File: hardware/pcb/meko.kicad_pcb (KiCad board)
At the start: 2 copper layers, 282 parts, among them IC1 MCP16502AB, IC2 MAYA-W386-00B, IC3 TAC5212, J1 Conn_01x02_Pin, J2 Conn_ARM_JTAG_SWD_10, J3 USB_C_Receptacle_USB2.0_16P, J4 PJ-342, J5 PJ-242, J6 Micro_SD_Card_Det2, J7 Micro_SD_Card_Det1, J8 503480-1000, SW1 SW_Push_Shielded, SW2 SW_Push_Shielded, SW3 SW_Push_Shielded, SW4 SW_Push_Shielded, SW5 SW_Push_Shielded, U1 SAMA7D65-4HB, U2 MT41K256M16TW, U3 TPS7A2033PDBV, U4 BQ25640, U5 MAX17260, U6 ECMF02-2AMX6, U7 DRV2605LDGS, Y1 24MHz, Y2 32kHz768, Y3 32kHz768

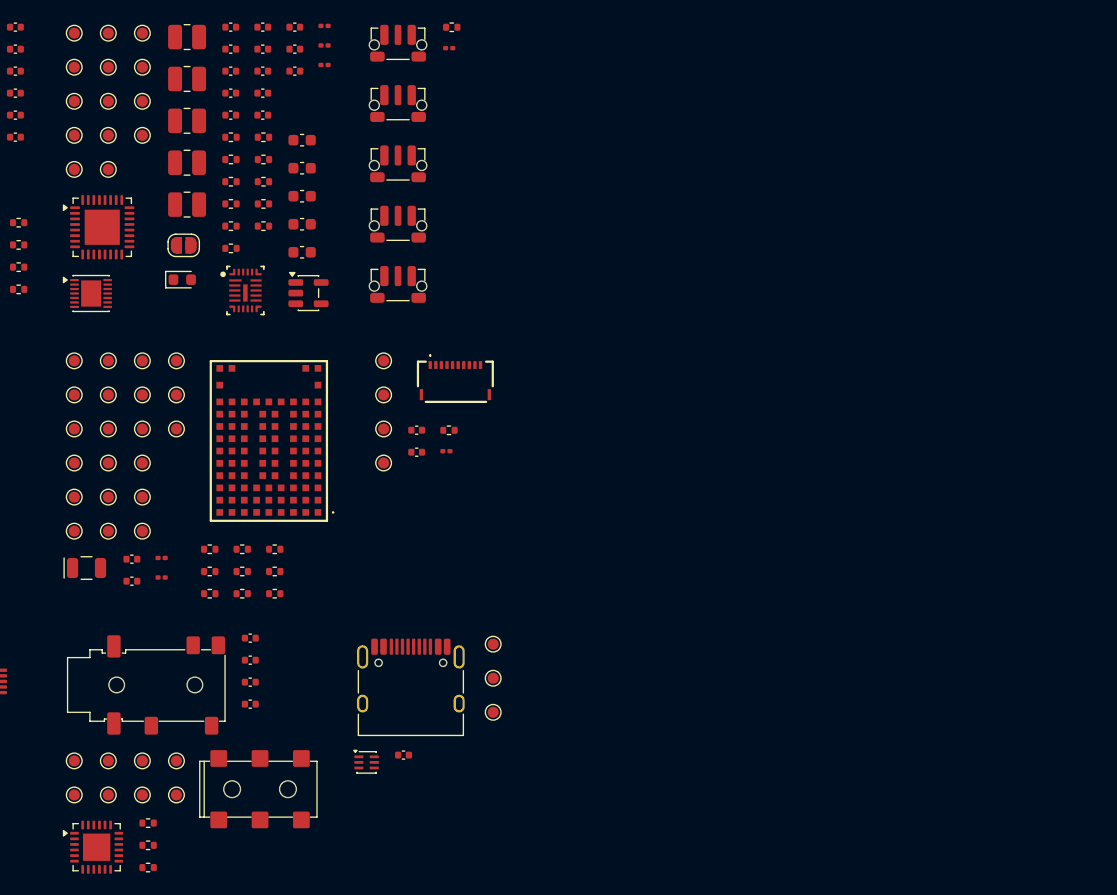
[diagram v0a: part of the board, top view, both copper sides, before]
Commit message: fixed 3.5mm footprint
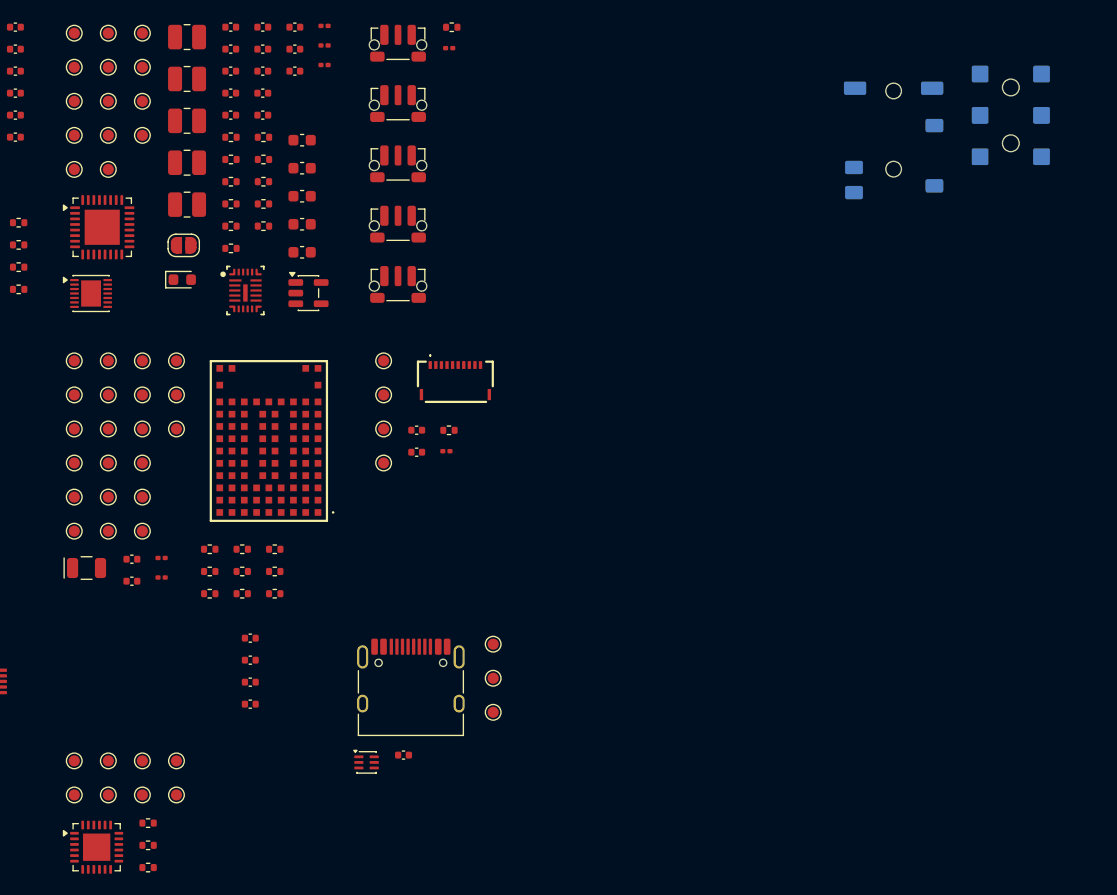
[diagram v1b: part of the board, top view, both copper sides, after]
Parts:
- J4, J5: moved to B.Cu
- moved J5 90.3 mm to (177.3, 61.5), turned to -90 degrees
- moved J4 77.8 mm to (166.8, 66.4), turned to -90 degrees

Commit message: mucking around with layout
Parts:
- IC3, J7: moved to B.Cu
- moved J7 141.6 mm to (205.7, 101.1), turned to -90 degrees
- moved IC2 129.1 mm to (239.4, 78.8)
- moved J6 113.5 mm to (187.8, 60.3), turned to 180 degrees
- moved IC3 96.4 mm to (174.0, 71.1), turned to 180 degrees
- moved U1 88.8 mm to (187.8, 81.5), turned to 0 degrees
- moved R42 88.3 mm to (168.3, 72.8)
- moved R41 88.3 mm to (168.3, 70.9)
- moved J8 79.8 mm to (206.4, 73.2), turned to -90 degrees
- moved U2 69.6 mm to (174.5, 97.9)
- moved J3 63.5 mm to (185.9, 125.7)
- moved J5 0.76 mm to (176.6, 61.5)
- moved J4 0.76 mm to (166.1, 66.3)

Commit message: doing layout
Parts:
- J3, SW2, SW3, SW4, SW5: moved to B.Cu
- moved SW5 138.4 mm to (213.7, 181.0), turned to -90 degrees
- moved SW3 122.6 mm to (213.8, 147.8), turned to -90 degrees
- moved SW4 118.2 mm to (166.8, 181.0), turned to 90 degrees
- moved SW2 118.0 mm to (213.7, 135.6), turned to -90 degrees
- moved J3 72.8 mm to (190.3, 198.4), turned to 180 degrees
- moved C100 43.9 mm to (78.9, 44.6)
- moved C101 43.9 mm to (75.4, 32.9)
- moved C102 43.9 mm to (81.0, 28.6)
- moved C103 43.9 mm to (78.9, 47.1)
- moved C104 43.9 mm to (75.4, 34.9)
- moved C105 43.9 mm to (81.0, 30.4)
- moved C109 43.9 mm to (63.7, 74.6)
- moved C110 43.9 mm to (63.7, 76.6)
- moved C111 43.9 mm to (66.4, 74.5)
- moved C112 43.9 mm to (66.4, 76.3)
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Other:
- board outline added: 50.2 x 77.2 mm

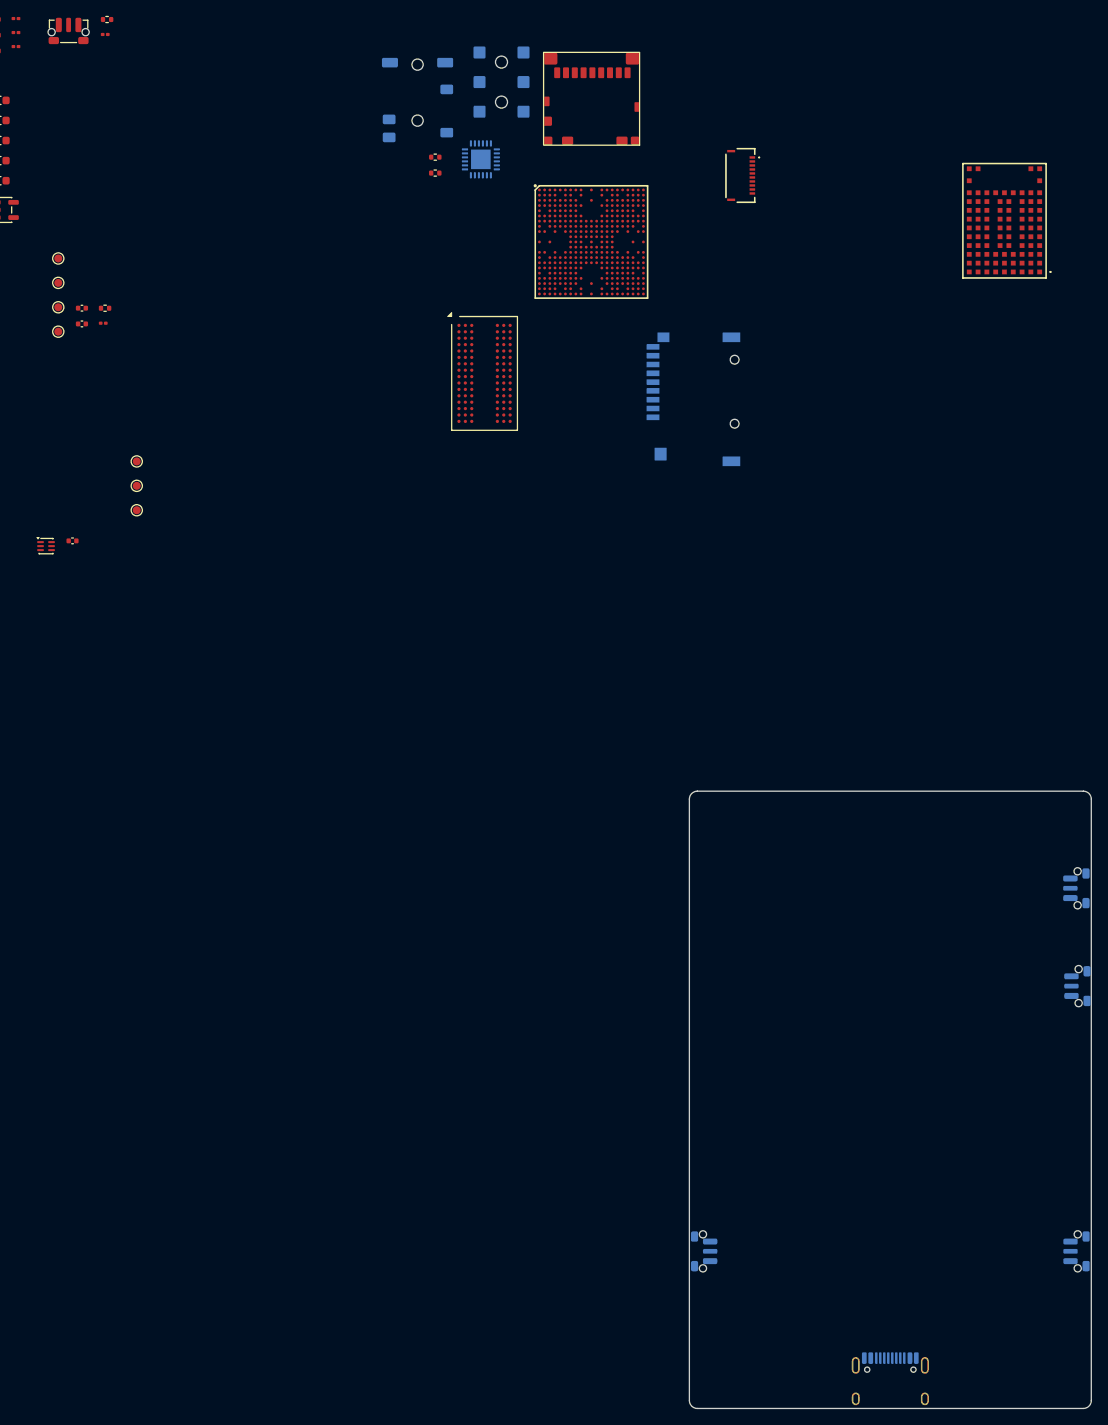
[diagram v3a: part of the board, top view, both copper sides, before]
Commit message: positioned buttons, jacks, and usb
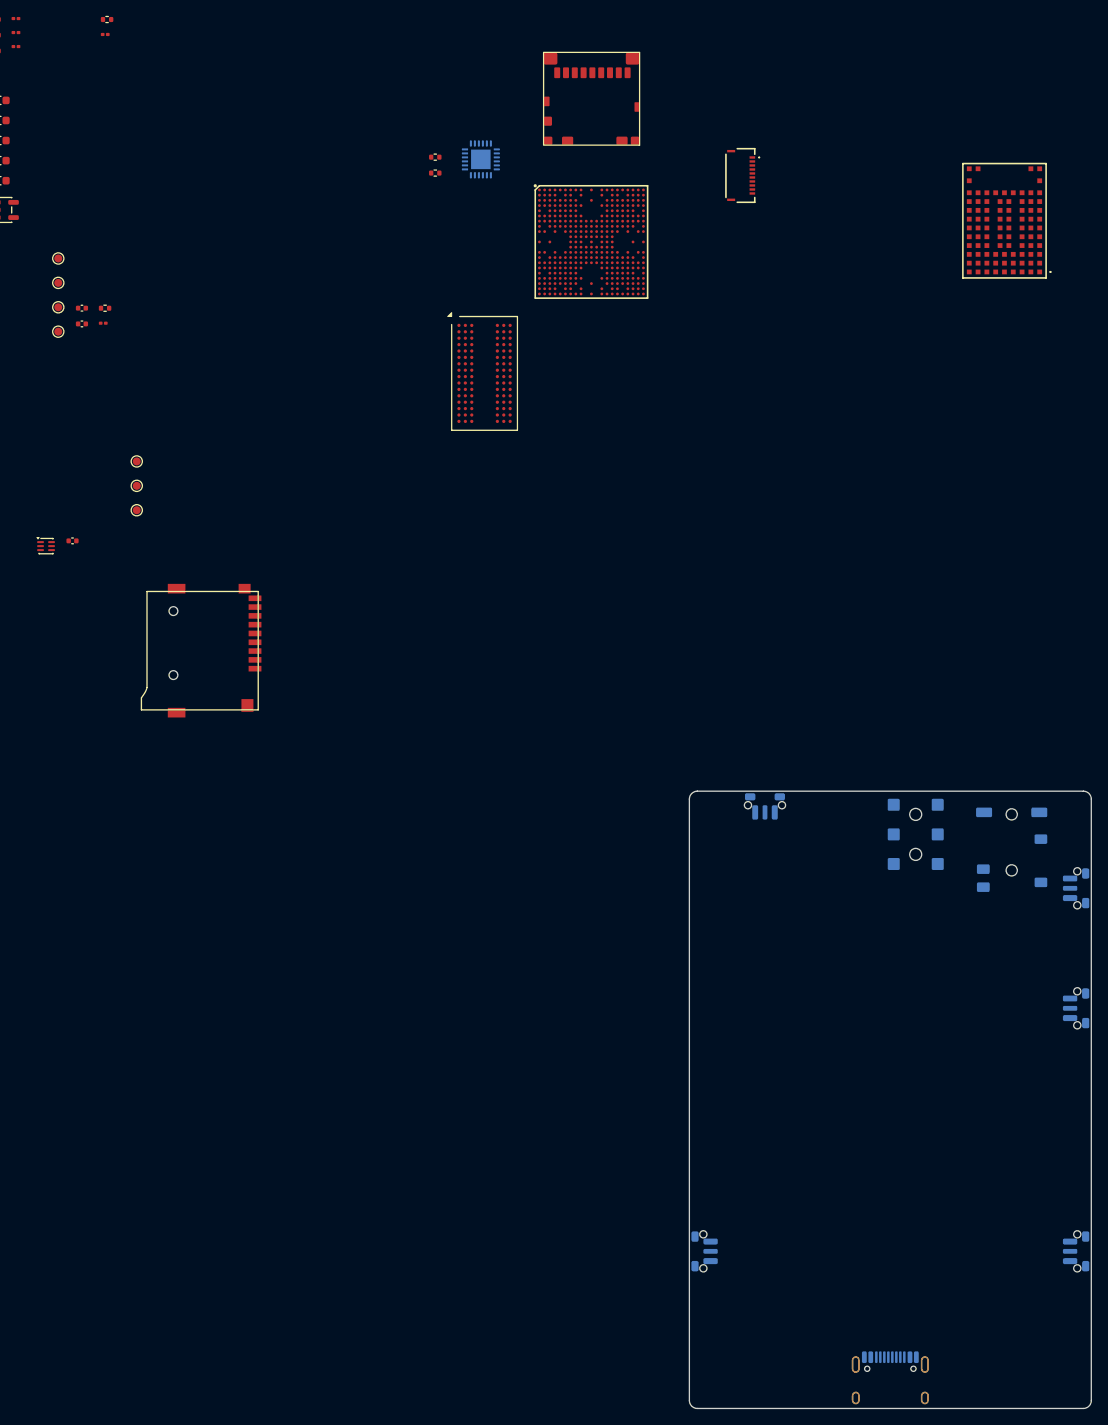
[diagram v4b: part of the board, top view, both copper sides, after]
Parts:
- J7: moved to F.Cu
- SW1: moved to B.Cu
- moved SW1 130.1 mm to (174.6, 125.2)
- moved J4 119.6 mm to (205.4, 133.3)
- moved J5 107.3 mm to (193.4, 128.8)
- moved J7 76.9 mm to (100.6, 105.9)
- moved SW3 2.78 mm to (213.6, 150.6)
- moved J3 0.11 mm to (190.3, 198.2)
- moved SW4 0.05 mm to (166.9, 181.0)
- moved SW5 0.05 mm to (213.6, 181.0)
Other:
- copper layers 2 -> 6

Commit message: more layour
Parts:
- IC2: value MAYA-W386-00B -> MAYAW38300B; moved to B.Cu
- J6, J7, J8, U1, U2: moved to B.Cu
- moved J6 168.6 mm to (205.1, 193.9)
- moved U2 142.4 mm to (269.6, 129.2), turned to 90 degrees
- moved U1 133.3 mm to (253.2, 142.6), turned to -90 degrees
- moved J7 117.2 mm to (175.1, 196.4), turned to 180 degrees
- moved IC2 114.2 mm to (208.2, 166.3), turned to 90 degrees
- moved IC3 107.1 mm to (225.8, 107.2)
- moved J8 97.0 mm to (180.6, 143.1)

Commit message: vendored in a bunch of footprints
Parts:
- IC2: value MAYAW38300B -> MAYA-W386-00B
- J3: footprint PCM_ckl-connector:USB_C_Receptacle_HRO_TYPE-C-31-M-12 -> ckl:USB_C_Receptacle_HRO_TYPE-C-31-M-12
- J4: footprint PCM_ckl-connector:Jack_3.5mm_SHOUHAN_PJ-342 -> ckl:Jack_3.5mm_SHOUHAN_PJ-342
- J6: footprint PCM_ckl-connector:microSD_SOFNG_TF-008 -> ckl:microSD_SOFNG_TF-008
- J7: footprint PCM_ckl-connector:microSD_XYECONN_TF-015-ZYD9AH185 -> ckl:microSD_XYECONN_TF-015-ZYD9AH185
- U2: footprint Package_BGA:Micron_FBGA-96_8x14mm_Layout9x16_P0.8mm -> MT41K256M16TW:Micron_FBGA-96_8x14mm_Layout9x16_P0.8mm
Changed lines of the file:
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@@
 		(capping no)
 		(filling no)
-		(zone_defaults)
 		(pcbplotparams
 			(layerselection 0x00000000_00000000_55555555_5755f5ff)
@@
 		)
 	)
-	(footprint "PCM_ckl-connector:microSD_SOFNG_TF-008"
+	(footprint "ckl:microSD_SOFNG_TF-008"
 		(layer "B.Cu")
 		(at 205.1125 193.95 180)
@@
 		(sheetname "/SD Cards/")
 		(sheetfile "sd.kicad_sch")
+		(units
+			(unit
+				(name "A")
+				(pins "1" "2" "3" "4" "5" "6" "7" "8" "10" "9" "SH")
+			)
+		)
 		(attr smd)
 		(duplicate_pad_numbers_are_jumpers no)
-		(fp_poly
-			(pts
-				(xy 6 -2.55) (xy 6 9.05) (xy -6 9.05) (xy -6 -2.55)
-			)
+		(fp_rect
+			(start -6 9.05)
+			(end 6 -2.55)
 			(stroke
 				(width 0.1)
@@
 			(layer "Dwgs.User")
 		)
-		(fp_poly
-			(pts
-				(xy 6.4 -3) (xy 6.4 9.4) (xy -6.4 9.4) (xy -6.4 -3)
-			)
+		(fp_rect
+			(start -6.4 9.4)
+			(end 6.4 -3)
 			(stroke
 				(width 0.05)
@@
 		)
 		(pad "6" smd roundrect
-			(at -2.300001 0 180)
+			(at -2.3 0 180)
 			(size 0.75 1.35)
 			(layers "B.Cu" "B.Mask" "B.Paste")
@@
 		)
 		(pad "8" smd roundrect
-			(at -4.500001 0 180)
+			(at -4.5 0 180)
 			(size 0.75 1.35)
 			(layers "B.Cu" "B.Mask" "B.Paste")
@@
 			(thermal_bridge_angle 45)
 		)
-		(pad "11" smd roundrect
+		(pad "SH" smd roundrect
 			(at -5.6675 4.28 180)
 			(size 0.615 1.2)
 			(layers "B.Cu" "B.Mask" "B.Paste")
 			(roundrect_rratio 0.15)
+			(net "GND")
+			(pinfunction "SHIELD_SH")
+			(pintype "passive")
 			(thermal_bridge_angle 45)
 		)
-		(pad "11" smd roundrect
+		(pad "SH" smd roundrect
 			(at -5.4375 8.505 180)
 			(size 1.075 1.05)
 			(layers "B.Cu" "B.Mask" "B.Paste")
 			(roundrect_rratio 0.15)
+			(net "GND")
+			(pinfunction "SHIELD_SH")
+			(pintype "passive")
 			(thermal_bridge_angle 45)
 		)
-		(pad "11" smd roundrect
+		(pad "SH" smd roundrect
 			(at -5.125 -1.77 180)
 			(size 1.7 1.5)
 			(layers "B.Cu" "B.Mask" "B.Paste")
 			(roundrect_rratio 0.15)
+			(net "GND")
+			(pinfunction "SHIELD_SH")
+			(pintype "passive")
 			(thermal_bridge_angle 45)
 		)
-		(pad "11" smd roundrect
+		(pad "SH" smd roundrect
 			(at -3.8 8.505 180)
 			(size 1.4 1.05)
 			(layers "B.Cu" "B.Mask" "B.Paste")
 			(roundrect_rratio 0.15)
+			(net "GND")
+			(pinfunction "SHIELD_SH")
+			(pintype "passive")
 			(thermal_bridge_angle 45)
 		)
-		(pad "11" smd roundrect
+		(pad "SH" smd roundrect
 			(at 3 8.505 180)
 			(size 1.4 1.05)
 			(layers "B.Cu" "B.Mask" "B.Paste")
 			(roundrect_rratio 0.15)
+			(net "GND")
+			(pinfunction "SHIELD_SH")
+			(pintype "passive")
 			(thermal_bridge_angle 45)
 		)
-		(pad "11" smd roundrect
+		(pad "SH" smd roundrect
 			(at 5.125 -1.77 180)
 			(size 1.7 1.5)
 			(layers "B.Cu" "B.Mask" "B.Paste")
 			(roundrect_rratio 0.15)
+			(net "GND")
+			(pinfunction "SHIELD_SH")
+			(pintype "passive")
 			(thermal_bridge_angle 45)
 		)
-		(pad "11" smd roundrect
+		(pad "SH" smd roundrect
 			(at 5.4375 8.505 180)
 			(size 1.075 1.05)
 			(layers "B.Cu" "B.Mask" "B.Paste")
 			(roundrect_rratio 0.15)
+			(net "GND")
+			(pinfunction "SHIELD_SH")
+			(pintype "passive")
 			(thermal_bridge_angle 45)
 		)
-		(pad "11" smd roundrect
+		(pad "SH" smd roundrect
 			(at 5.6125 3.58 180)
 			(size 0.725 1.2)
 			(layers "B.Cu" "B.Mask" "B.Paste")
 			(roundrect_rratio 0.15)
+			(net "GND")
+			(pinfunction "SHIELD_SH")
+			(pintype "passive")
 			(thermal_bridge_angle 45)
 		)
@@
 					(xy 200.0125 194.95) (xy 200.0125 192.35) (xy 210.2625 192.35) (xy 210.2625 194.95) (xy 211.1125 194.95)
 					(xy 211.1125 190.3) (xy 210.4625 190.3) (xy 210.4625 189.05) (xy 211.1125 189.05) (xy 211.1125 186)
-					(xy 210.512501 186) (xy 210.5125 186.35) (xy 199.7625 186.35) (xy 199.7625 186) (xy 199.1125 186)
-					(xy 199.1125 187.3) (xy 200.1625 187.299999) (xy 200.162499 188.5) (xy 199.1125 188.5) (xy 199.1125 189.75)
-					(xy 199.8625 189.75) (xy 199.862499 191) (xy 199.1125 191) (xy 199.1125 194.95)
+					(xy 210.5125 186) (xy 210.5125 186.35) (xy 199.7625 186.35) (xy 199.7625 186) (xy 199.1125 186)
+					(xy 199.1125 187.3) (xy 200.1625 187.3) (xy 200.1625 188.5) (xy 199.1125 188.5) (xy 199.1125 189.75)
+					(xy 199.8625 189.75) (xy 199.8625 191) (xy 199.1125 191) (xy 199.1125 194.95)
 				)
 			)
@@
 			)
 		)
-		(property "Value" "MAYAW38300B"
+		(property "Value" "MAYA-W386-00B"
 			(at 0 0 90)
 			(layer "B.SilkS")
@@
 		(sheetname "/Wireless/")
 		(sheetfile "wireless.kicad_sch")
+		(units
+			(unit
+				(name "A")
+				(pins "E2" "D4" "D5" "C3" "C7" "D7" "C8" "D3" "E3" "E7" "J9" "J7" "G8"
+					"G9" "H8" "H9" "E8" "D8" "F8" "F9" "E9" "B9" "C9" "D9" "C5" "C4" "C6"
+					"B6" "G7" "F7" "J8" "J3" "A4" "B4" "B3" "A3" "B5" "A5" "A2" "K2" "K3"
+					"K4" "K5" "K6" "K7" "K8" "H5" "H4" "L1" "M1" "M2" "M8" "A1" "M9" "B2"
+					"B8" "E4" "E5" "A9" "F4" "F5" "A7" "B7" "D1" "H1" "J1" "E1" "G1" "F1"
+					"C1" "J2" "H3" "H2" "G3" "G2" "F3" "F2" "H7" "L9" "K9" "K1" "J4" "G5"
+					"J5" "G4" "B1" "D2" "C2" "A8" "A6"
+				)
+			)
+		)
 		(attr smd)
 		(duplicate_pad_numbers_are_jumpers no)
@@
 		)
 	)
-	(footprint "PCM_ckl-connector:microSD_XYECONN_TF-015-ZYD9AH185"
+	(footprint "ckl:microSD_XYECONN_TF-015-ZYD9AH185"
 		(layer "B.Cu")
 		(at 175.12 196.3725 180)
@@
 		(sheetname "/SD Cards/")
 		(sheetfile "sd.kicad_sch")
+		(units
+			(unit
+				(name "A")
+				(pins "1" "2" "3" "4" "5" "6" "7" "8" "9" "SH")
+			)
+		)
 		(attr smd)
 		(duplicate_pad_numbers_are_jumpers no)
@@
 		(fp_curve
 			(pts
-				(xy 4.6 -3.3) (xy 5.100001 -3.4) (xy 5.6 -3.8) (xy 5.9 -4)
+				(xy 4.6 -3.3) (xy 5.1 -3.4) (xy 5.6 -3.8) (xy 5.9 -4)
 			)
 			(stroke
@@
 		)
 		(fp_line
-			(start 7.799999 -0.8)
+			(start 7.8 -0.8)
 			(end 8.6 -0.8)
 			(stroke
@@
 		)
 		(fp_line
-			(start 7.799999 -0.8)
-			(end 7.799999 -4.2)
+			(start 7.8 -0.8)
+			(end 7.8 -4.2)
 			(stroke
 				(width 0.05)
@@
 		)
 		(fp_line
-			(start 7.799999 -4.2)
+			(start 7.8 -4.2)
 			(end -7.6 -4.2)
 			(stroke
@@
 		)
 		(pad "" np_thru_hole circle
-			(at -4.950001 0 180)
+			(at -4.95 0 180)
 			(size 1.1 1.1)
 			(drill 1.1)
@@
 			(thermal_bridge_angle 45)
 		)
-		(pad "10" smd rect
+		(pad "SH" smd rect
 			(at -7.75 0.4 180)
 			(size 1.2 2.2)
 			(layers "B.Cu" "B.Mask" "B.Paste")
+			(net "GND")
+			(pinfunction "SHIELD_SH")
+			(pintype "passive")
 			(thermal_bridge_angle 45)
 		)
-		(pad "10" smd rect
+		(pad "SH" smd rect
 			(at -7.75 8.9 180)
 			(size 1.2 1.5)
 			(layers "B.Cu" "B.Mask" "B.Paste")
+			(net "GND")
+			(pinfunction "SHIELD_SH")
+			(pintype "passive")
 			(thermal_bridge_angle 45)
 		)
-		(pad "10" smd rect
+		(pad "SH" smd rect
 			(at 6.85 9.25 180)
 			(size 1.6 1.5)
 			(layers "B.Cu" "B.Mask" "B.Paste")
+			(net "GND")
+			(pinfunction "SHIELD_SH")
+			(pintype "passive")
 			(thermal_bridge_angle 45)
 		)
-		(pad "10" smd rect
+		(pad "SH" smd rect
 			(at 7.75 0.4 180)
 			(size 1.2 2.2)
 			(layers "B.Cu" "B.Mask" "B.Paste")
+			(net "GND")
+			(pinfunction "SHIELD_SH")
+			(pintype "passive")
 			(thermal_bridge_angle 45)
 		)
@@
 			(polygon
 				(pts
-					(xy 182.52 200.3725) (xy 182.52 199.6725) (xy 169.22 199.672499) (xy 169.22 204.4725) (xy 182.52 204.4725)
+					(xy 182.52 200.3725) (xy 182.52 199.6725) (xy 169.22 199.6725) (xy 169.22 204.4725) (xy 182.52 204.4725)
 				)
 			)
@@
 		(sheetname "/Audio/")
 		(sheetfile "audio.kicad_sch")
+		(units
+			(unit
+				(name "A")
+				(pins "S" "R2" "R1" "R1N" "T" "TN")
+			)
+		)
 		(attr smd)
 		(duplicate_pad_numbers_are_jumpers no)
@@
 		)
 	)
-	(footprint "PCM_ckl-connector:Jack_3.5mm_SHOUHAN_PJ-342"
+	(footprint "ckl:Jack_3.5mm_SHOUHAN_PJ-342"
 		(layer "B.Cu")
 		(at 205.422907 133.34 -90)
@@
 		)
 		(embedded_fonts no)
-		(model "${KICAD10_3RD_PARTY}/3dmodels/com_github_cheyao_ckl/AUDIO-SMD_PJ-342-141.step"
+		(model "${KIPRJMOD}/lib/ckl/AUDIO-SMD_PJ-342-141.step"
 			(offset
 				(xyz -11.4 0 2.3)
@@
 		)
 	)
-	(footprint "Package_BGA:Micron_FBGA-96_8x14mm_Layout9x16_P0.8mm"
+	(footprint "MT41K256M16TW:Micron_FBGA-96_8x14mm_Layout9x16_P0.8mm"
 		(layer "B.Cu")
 		(at 269.62 129.179999 90)
@@
 		)
 		(embedded_fonts no)
-		(model "${KICAD10_3DMODEL_DIR}/Package_BGA.3dshapes/Micron_FBGA-96_8x14mm_Layout9x16_P0.8mm.step"
+		(model "${KIPRJMOD}/lib/MT41K256M16TW/Micron_FBGA-96_8x14mm_Layout9x16_P0.8mm.step"
 			(offset
 				(xyz 0 0 0)
@@
 		)
 	)
-	(footprint "PCM_ckl-connector:USB_C_Receptacle_HRO_TYPE-C-31-M-12"
+	(footprint "ckl:USB_C_Receptacle_HRO_TYPE-C-31-M-12"
 		(layer "B.Cu")
 		(at 190.252893 198.242893 180)
@@
 		)
 		(embedded_fonts no)
-		(model "${KICAD10_3RD_PARTY}/3dmodels/com_github_cheyao_ckl/USB_C_Receptacle_HRO_TYPE-C-31-M-12.step"
+		(model "${KIPRJMOD}/lib/ckl/USB_C_Receptacle_HRO_TYPE-C-31-M-12.step"
 			(offset
 				(xyz 0 -1.05 0)
